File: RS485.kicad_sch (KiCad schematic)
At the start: 0 parts

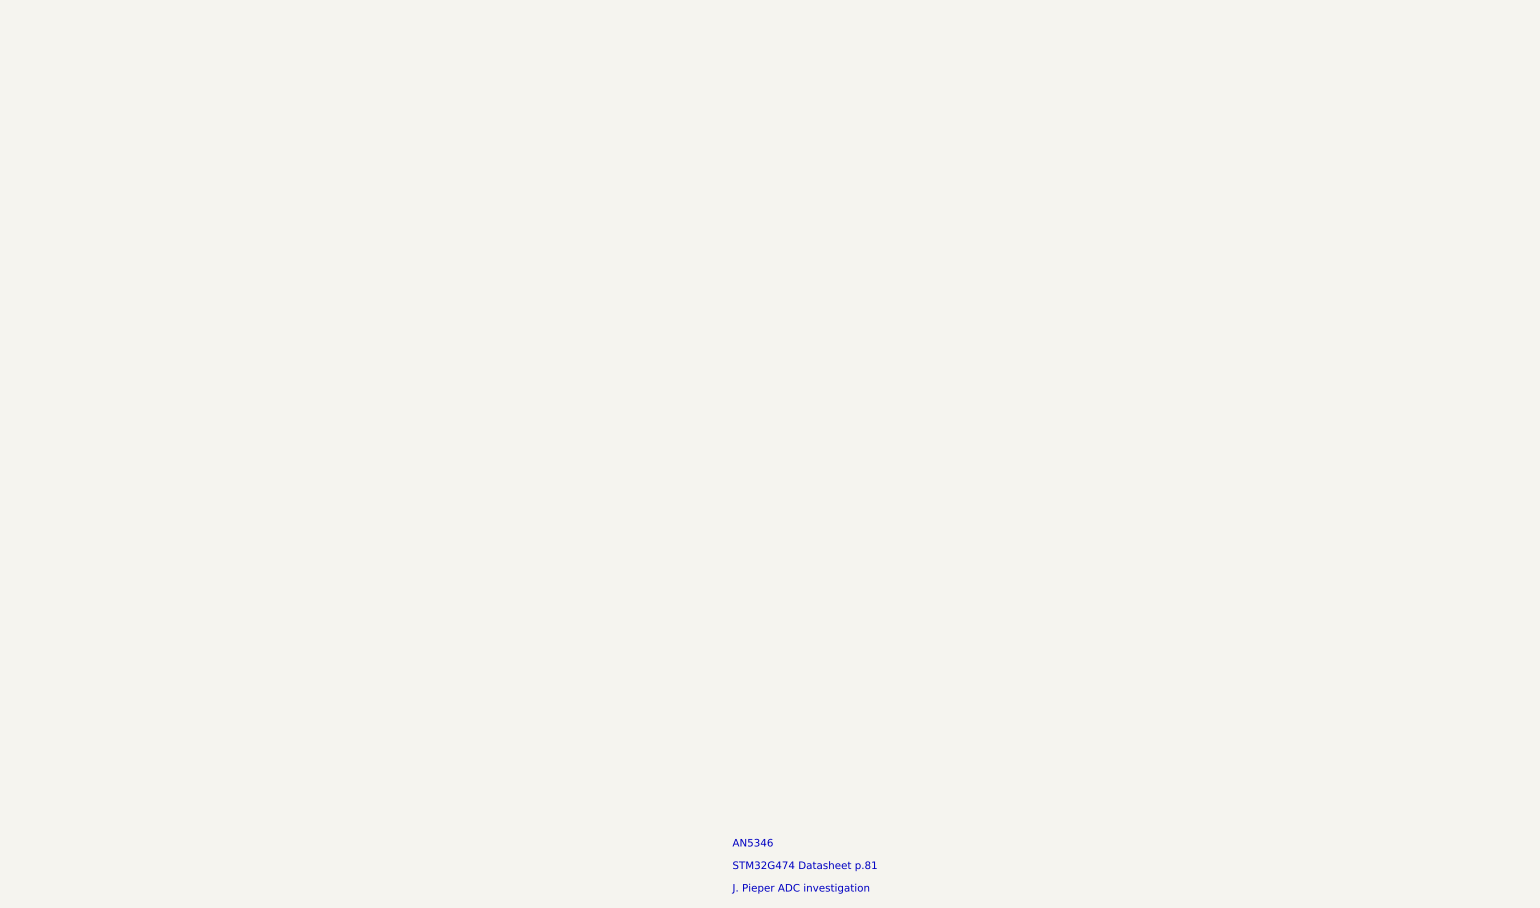
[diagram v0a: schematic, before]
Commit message: [Schematic][Added] Project Architecture, connectors
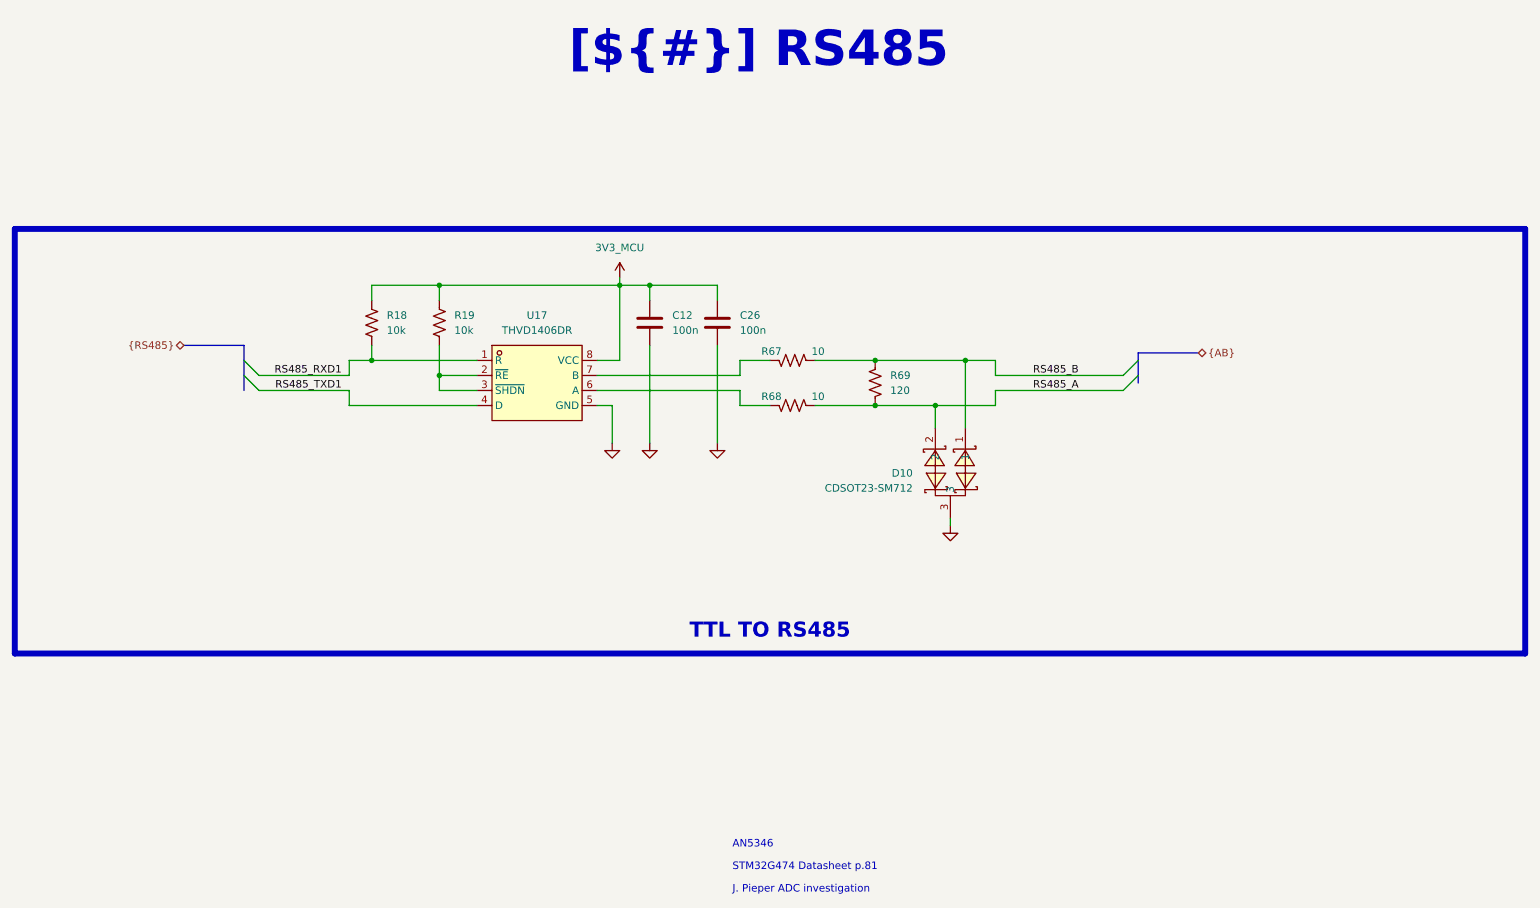
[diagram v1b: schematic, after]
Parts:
- added C12, C26: 100n, Capacitor_SMD:C_0603_1608Metric, symbol Device:C
- added D10: CDSOT23-SM712, easyeda2kicad:SOT-23_L2.9-W1.3-P1.90-LS2.4-BR, symbol easyeda2kicad:CDSOT23-SM712
- added R18, R19: 10k, Resistor_SMD:R_0402_1005Metric, symbol Device:R_US
- added R67, R68: 10, Resistor_SMD:R_0603_1608Metric, symbol Device:R_US
- added R69: 120, Resistor_SMD:R_0603_1608Metric, symbol Device:R_US
- added U17: THVD1406DR, easyeda2kicad:SOIC-8_L4.9-W3.9-P1.27-LS6.0-BL, symbol easyeda2kicad:THVD1406DR
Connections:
- new net: R67.1, U17.7 (B)
- new net: R19.2, U17.2 (~{RE}), U17.3 (~{SHDN})
- new net: R68.1, U17.6 (A)
- new net 3V3_MCU: C12.1, C26.1, R18.1, R19.1, U17.8 (VCC)
- new net GND: C12.2, C26.2, D10.3, U17.5 (GND)
- new net RS485_A: D10.2, R68.2, R69.2
- new net RS485_B: D10.1, R67.2, R69.1
- new net RS485_RXD1: R18.2, U17.1 (R)
- new net RS485_TXD1: U17.4 (D)
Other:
- title: MCU -> RS485

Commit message: [Schematic][Added] Connectors and first PCB layout
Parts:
- C12, C26: footprint Capacitor_SMD:C_0603_1608Metric -> Capacitor_SMD:C_0402_1005Metric
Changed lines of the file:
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@@
 			)
 		)
-		(property "Footprint" "Capacitor_SMD:C_0603_1608Metric"
+		(property "Footprint" "Capacitor_SMD:C_0402_1005Metric"
 			(at 129.2352 77.47 0)
 			(effects
@@
 			)
 		)
-		(property "Footprint" "Capacitor_SMD:C_0603_1608Metric"
+		(property "Footprint" "Capacitor_SMD:C_0402_1005Metric"
 			(at 140.6652 77.47 0)
 			(effects

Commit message: [PCB][Added] Gerber, CPL, BOM ready
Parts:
- C12, C26: LCSC (none) -> C77020
- D10: LCSC (none) -> C404012
- R18, R19: LCSC (none) -> C25744
- R67, R68: LCSC (none) -> C313648
- R69: LCSC (none) -> C22787
- U17: LCSC (none) -> C5215918
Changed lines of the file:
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@@
+			)
+		)
+		(property "LCSC" "C404012"
+			(at 172.72 99.06 0)
+			(effects
+				(font
+					(size 1.27 1.27)
+				)
+				(hide yes)
 			)
 		)
@@
 			)
 		)
+		(property "LCSC" "C313648"
+			(at 148.844 78.486 0)
+			(effects
+				(font
+					(size 1.27 1.27)
+				)
+				(hide yes)
+			)
+		)
 		(pin "1"
 		)
@@
 			)
 		)
+		(property "LCSC" "C77020"
+			(at 132.08 72.3899 0)
+			(effects
+				(font
+					(size 1.27 1.27)
+				)
+				(hide yes)
+			)
+		)
 		(pin "1"
 		)
@@
 			)
 		)
+		(property "LCSC" "C25744"
+			(at 95.25 72.3899 0)
+			(effects
+				(font
+					(size 1.27 1.27)
+				)
+				(hide yes)
+			)
+		)
 		(pin "1"
 		)
@@
 			)
 		)
+		(property "LCSC" "C22787"
+			(at 168.91 82.5499 0)
+			(effects
+				(font
+					(size 1.27 1.27)
+				)
+				(hide yes)
+			)
+		)
 		(pin "1"
 		)
@@
 			)
 		)
+		(property "LCSC" "C25744"
+			(at 83.82 72.3899 0)
+			(effects
+				(font
+					(size 1.27 1.27)
+				)
+				(hide yes)
+			)
+		)
 		(pin "1"
 		)
@@
 			)
 		)
+		(property "LCSC" "C77020"
+			(at 143.51 72.3899 0)
+			(effects
+				(font
+					(size 1.27 1.27)
+				)
+				(hide yes)
+			)
+		)
 		(pin "1"
 		)
@@
 			)
 		)
+		(property "LCSC" "C5215918"
+			(at 109.22 72.39 0)
+			(effects
+				(font
+					(size 1.27 1.27)
+				)
+				(hide yes)
+			)
+		)
 		(pin "1"
 		)
@@
 			)
 		)
+		(property "LCSC" "C313648"
+			(at 148.844 86.106 0)
+			(effects
+				(font
+					(size 1.27 1.27)
+				)
+				(hide yes)
+			)
+		)
